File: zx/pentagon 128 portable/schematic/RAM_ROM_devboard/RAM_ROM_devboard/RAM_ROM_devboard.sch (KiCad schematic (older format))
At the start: 8 parts, among them IC1 IS62C1024AL-35QLI, IC2 SN74AHCT04D, J1 Conn_02x14_Odd_Even, J2 8432-11B1-RK-TP, J3 Conn_02x08_Odd_Even, J4 Conn_02x04_Odd_Even, J5 Conn_02x06_Odd_Even, J6 Conn_02x06_Odd_Even

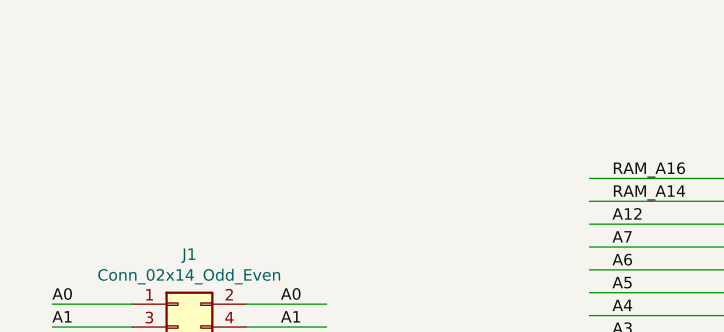
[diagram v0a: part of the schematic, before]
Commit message: updated focs, added Z80 devboard
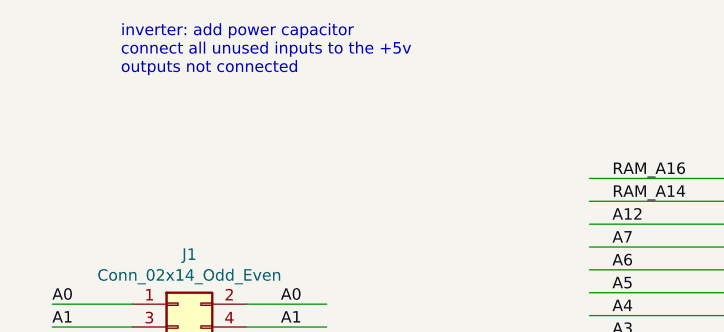
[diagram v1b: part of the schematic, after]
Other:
- note added: "inverter: add power capacitor\nconnect all unused inputs to the +5v\noutputs not connected"
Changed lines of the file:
@@
 	6050 4400 6050 4300
 Connection ~ 6050 4400
+Text Notes 1050 1200 0    50   ~ 0
+inverter: add power capacitor\nconnect all unused inputs to the +5v\noutputs not connected
 $EndSCHEMATC

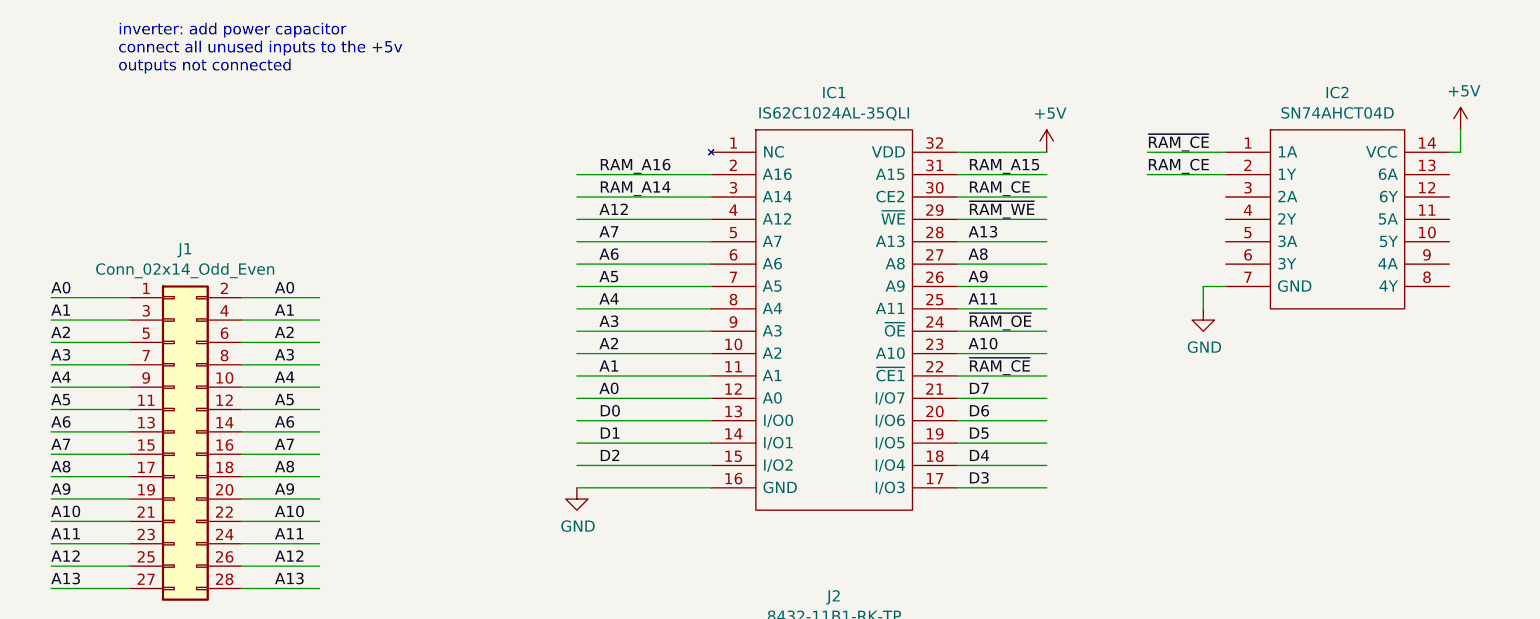
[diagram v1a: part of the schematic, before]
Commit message: added ZX Keyboard
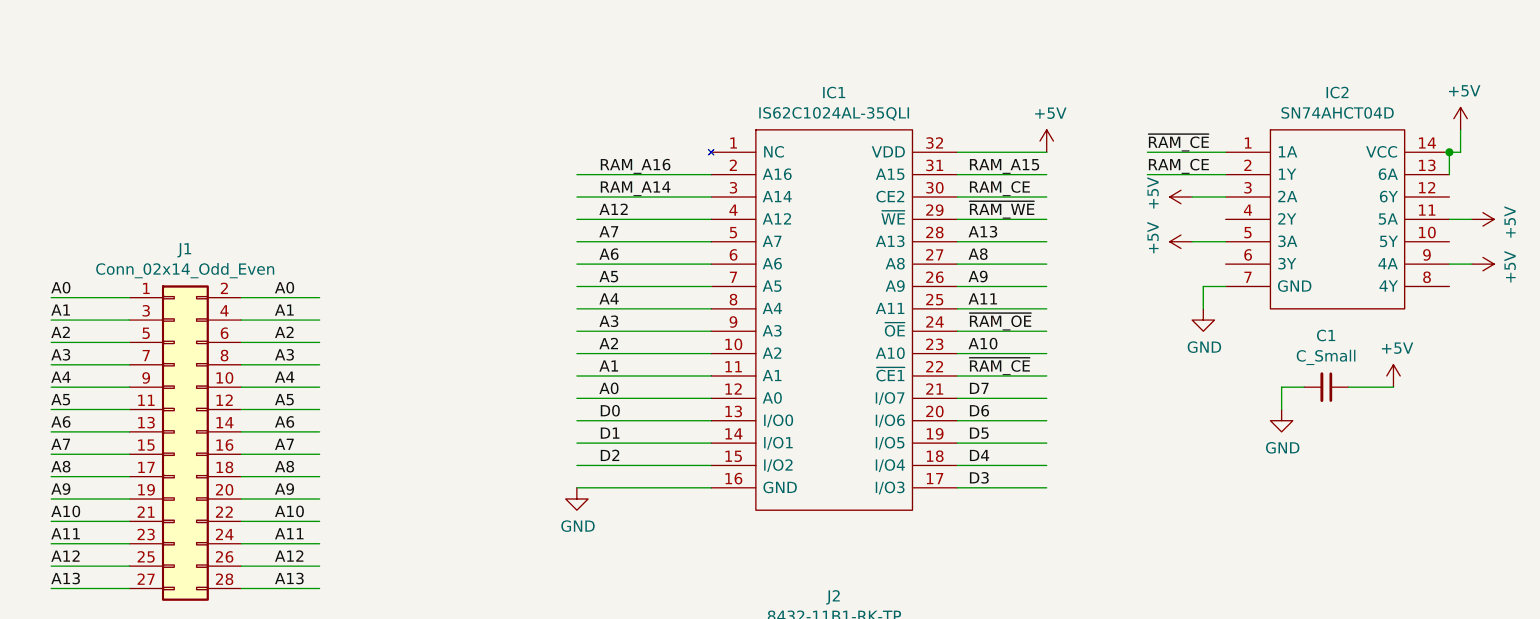
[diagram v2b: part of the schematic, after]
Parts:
- added C1: C_Small, Capacitor_SMD:C_0402_1005Metric, symbol Device:C_Small
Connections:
- wire segments 149 -> 157
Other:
- note removed: "inverter: add power capacitor\nconnect all unused inputs to the +5v\noutputs not connected"
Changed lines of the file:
@@
 	6050 4400 6050 4300
 Connection ~ 6050 4400
-Text Notes 1050 1200 0    50   ~ 0
-inverter: add power capacitor\nconnect all unused inputs to the +5v\noutputs not connected
+$Comp
+L power:+5V #PWR0109
+U 1 1 5F62EBF2
+P 5850 1750
+F 0 "#PWR0109" H 5850 1600 50  0001 C CNN
+F 1 "+5V" H 5865 1923 50  0000 C CNN
+F 2 "" H 5850 1750 50  0001 C CNN
+F 3 "" H 5850 1750 50  0001 C CNN
+	1    5850 1750
+	0    -1   -1   0
+$EndComp
+$Comp
+L power:+5V #PWR0110
+U 1 1 5F62F7B9
+P 5850 1950
+F 0 "#PWR0110" H 5850 1800 50  0001 C CNN
+F 1 "+5V" H 5865 2123 50  0000 C CNN
+F 2 "" H 5850 1950 50  0001 C CNN
+F 3 "" H 5850 1950 50  0001 C CNN
+	1    5850 1950
+	0    -1   -1   0
+$EndComp
+Wire Wire Line
+	6000 1950 5850 1950
+Wire Wire Line
+	6000 1750 5850 1750
+$Comp
+L power:+5V #PWR0111
+U 1 1 5F647A6C
+P 7100 1850
+F 0 "#PWR0111" H 7100 1700 50  0001 C CNN
+F 1 "+5V" H 7115 2023 50  0000 C CNN
+F 2 "" H 7100 1850 50  0001 C CNN
+F 3 "" H 7100 1850 50  0001 C CNN
+	1    7100 1850
+	0    1    1    0
+$EndComp
+$Comp
+L power:+5V #PWR0112
+U 1 1 5F6486F7
+P 7100 2050
+F 0 "#PWR0112" H 7100 1900 50  0001 C CNN
+F 1 "+5V" H 7115 2223 50  0000 C CNN
+F 2 "" H 7100 2050 50  0001 C CNN
+F 3 "" H 7100 2050 50  0001 C CNN
+	1    7100 2050
+	0    1    1    0
+$EndComp
+Wire Wire Line
+	7000 1650 7000 1550
+Connection ~ 7000 1550
+Wire Wire Line
+	7000 1850 7100 1850
+Wire Wire Line
+	7000 2050 7100 2050
+$Comp
+L Device:C_Small C1
+U 1 1 5F66D823
+P 6450 2600
+F 0 "C1" V 6221 2600 50  0000 C CNN
+F 1 "C_Small" V 6312 2600 50  0000 C CNN
+F 2 "Capacitor_SMD:C_0402_1005Metric" H 6450 2600 50  0001 C CNN
+F 3 "~" H 6450 2600 50  0001 C CNN
+	1    6450 2600
+	0    1    1    0
+$EndComp
+$Comp
+L power:GND #PWR0113
+U 1 1 5F66F725
+P 6250 2700
+F 0 "#PWR0113" H 6250 2450 50  0001 C CNN
+F 1 "GND" H 6255 2527 50  0000 C CNN
+F 2 "" H 6250 2700 50  0001 C CNN
+F 3 "" H 6250 2700 50  0001 C CNN
+	1    6250 2700
+	1    0    0    -1
+$EndComp
+$Comp
+L power:+5V #PWR0114
+U 1 1 5F670043
+P 6750 2600
+F 0 "#PWR0114" H 6750 2450 50  0001 C CNN
+F 1 "+5V" H 6765 2773 50  0000 C CNN
+F 2 "" H 6750 2600 50  0001 C CNN
+F 3 "" H 6750 2600 50  0001 C CNN
+	1    6750 2600
+	1    0    0    -1
+$EndComp
+Wire Wire Line
+	6550 2600 6750 2600
+Wire Wire Line
+	6350 2600 6250 2600
+Wire Wire Line
+	6250 2600 6250 2700
 $EndSCHEMATC
